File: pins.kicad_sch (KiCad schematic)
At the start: 10 parts, among them J2 AXK640347YG, J3 Conn_01x09, J6 Conn_01x40_Pin

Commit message: initial commit, not complete.
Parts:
- added C36, C37: 100n, Capacitor_SMD:C_0603_1608Metric_Pad1.08x0.95mm_HandSolder, symbol Device:C_Small
- added H1, H2, H3, H4: MountingHole_Pad, MountingHole:MountingHole_2.7mm_M2.5_DIN965_Pad_TopBottom, symbol Mechanical:MountingHole_Pad
- added JP1: Jumper_3_Open, Jumper:SolderJumper-3_P1.3mm_Open_RoundedPad1.0x1.5mm_NumberLabels, symbol Jumper:Jumper_3_Open
- added R30: 22k, Resistor_SMD:R_0603_1608Metric_Pad0.98x0.95mm_HandSolder, symbol Device:R_Small
- added R31: 12k, Resistor_SMD:R_0603_1608Metric_Pad0.98x0.95mm_HandSolder, symbol Device:R_Small
- added TP13: GP, TestPoint:TestPoint_Pad_D1.0mm, symbol Connector:TestPoint
- added U11: TXS0108EPW, Package_SO:TSSOP-20_4.4x6.5mm_P0.65mm, symbol Logic_LevelTranslator:TXS0108EPW
- added U8: TXS0102DCU, Package_SO:VSSOP-8_2.3x2mm_P0.5mm, symbol Logic_LevelTranslator:TXS0102DCU
- FB1: footprint Inductor_SMD:L_0603_1608Metric_Pad1.05x0.95mm_HandSolder -> Inductor_SMD:L_0805_2012Metric_Pad1.15x1.40mm_HandSolder
- J2: now not fitted; now left out of the parts list
- J3: footprint Connector_PinSocket_2.00mm:PinSocket_1x09_P2.00mm_Horizontal -> Connector_PinHeader_2.54mm:PinHeader_1x09_P2.54mm_Vertical; now fitted
- J6: now fitted; now in the parts list
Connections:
- net DISCAUDIO is gone; now on net BASEBAND_IN: J6.7 (Pin_7)
- net +5V: now also C37.1, U11.19 (VCCB), U8.7 (VCCB)
- net +5VD: now also J3.7 (Pin_7); no longer J3.2 (Pin_2)
- net 9V3: now also J6.38 (Pin_38)
- net AUDIO_IN: now also J3.4 (Pin_4), J6.33 (Pin_33); no longer J3.5 (Pin_5)
- net AUDIO_OUT_FILT: now also J3.3 (Pin_3), J6.34 (Pin_34); no longer J3.6 (Pin_6)
- net BASEBAND_IN: now also J3.2 (Pin_2); no longer J3.7 (Pin_7)
- net BASEBAND_OUT_FILT: now also J3.5 (Pin_5), JP1.2 (C); no longer J3.4 (Pin_4)
- net CH_Activity: now also U11.3 (A2); no longer J6.8 (Pin_8)
- net GND: now also J3.1 (Pin_1), C36.2, C37.2, H1.1, H2.1, H3.1, H4.1, R30.2, U11.11 (GND), U8.2 (GND); no longer J3.8 (Pin_8)
- net MCU_RX: now also TP13.1, U11.1 (A1), U8.5 (A1); no longer J3.1 (Pin_1)
- net OPT_CS: now also U11.9 (A8); no longer J6.30 (Pin_30)
- net PTT_IN: now also U11.7 (A6); no longer J3.9 (Pin_9)
- net PTT_OUT: now also U11.4 (A3), U8.4 (A2); no longer J3.3 (Pin_3)
- net RDY: now also U11.8 (A7); no longer J6.29 (Pin_29)
- net EXP_BD_REQ_5V: now reaches J6.10 (Pin_10)
- net EXP_BD_REQ_5V: now also U11.16 (B4)
- net EXP1_CS_5V: now reaches J6.11 (Pin_11)
- net EXP1_CS_5V: now also R31.2
- net GP4_IN_OUT_ACC8_5V: now reaches J6.12 (Pin_12)
- net GP4_IN_OUT_ACC8_5V: now also U11.15 (B5)
- net PTT_IN_5V: now reaches J6.23 (Pin_23)
- net PTT_IN_5V: now also U11.14 (B6)
- net Flat_Tx_Rtn: now reaches J6.31 (Pin_31)
- net Flat_Tx_Rtn: now also JP1.1 (A)
- net Tx_Aud_Rtn: now reaches J6.32 (Pin_32)
- net Tx_Aud_Rtn: now also JP1.3 (B)
- net GP1_IN_ACC3_5V: now reaches J6.9 (Pin_9)
- net GP1_IN_ACC3_5V: now also U11.17 (B3)
- net BUS+ renamed BUS+_5V
- net BUS+_5V: now also U11.20 (B1)
- new net: J3.6 (Pin_6), U8.1 (B2)
- new net: J3.8 (Pin_8), U8.8 (B1)
- new net +3V3: C36.1, U11.10 (OE), U11.2 (VCCA), U8.3 (VCCA), U8.6 (OE)
- new net CH_Activity_5V: J6.8 (Pin_8), U11.18 (B2)
- new net EXP1_CS: R30.1, R31.1
- new net EXP_BD_REQ: U11.5 (A4)
- new net GP4_IN_OUT_ACC8: U11.6 (A5)
- new net OPT_CS_5V: J6.30 (Pin_30), U11.12 (B8)
- new net RDY_5V: J6.29 (Pin_29), U11.13 (B7)
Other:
- note added: "All digital signals = 5V"
- note added: "VS_MIC VS_CS 9V3 VDD VS_AUDSEL Det_Aud_Snd Rx_Aud_Rtn Tx_Aud_Snd Tx_Aud_Rtn Flat_Tx_Rtn Opt_Bd_En Rdy/Req Rx_Aud_Snd ON INT_EXT_Vdd Key_Row Key_Col PTT Key_Intrp VS_INT RST* LED_EN OFF_BATT_DATA_OUT VS_GAINSEL SrD_Rtn SrD_Snd R/W* CS* DB0 DB1 DB2 DB3 EXT_BD_PTT DB4 DB5 145mV RMS @25kHz / 72mV RMS @12.5kHz DB6 DB7 A0 SCK_Snd VS_RAC Gnd, Pysically close pin to case"
- moved on the sheet: FB1, TP10, TP5, TP6, TP7, TP8, TP9

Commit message: .
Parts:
- removed TP10, TP13, TP6, TP8, TP9: GP, TestPoint:TestPoint_Pad_D1.0mm, symbol Connector:TestPoint
- added Q1: BC817, Package_TO_SOT_SMD:SOT-23, symbol Transistor_BJT:BC817
- added R32: 3k3, Resistor_SMD:R_0603_1608Metric_Pad0.98x0.95mm_HandSolder, symbol Device:R_Small
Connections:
- net +5VD: no longer TP5.1
- net GND: now also Q1.2 (E)
- net MCU_RX: now also TP5.1
- net at J3.9 (Pin_9): now also Q1.3 (C)
- new net: Q1.1 (B), R32.2
- new net BASEBAND_BYPASS: R32.1

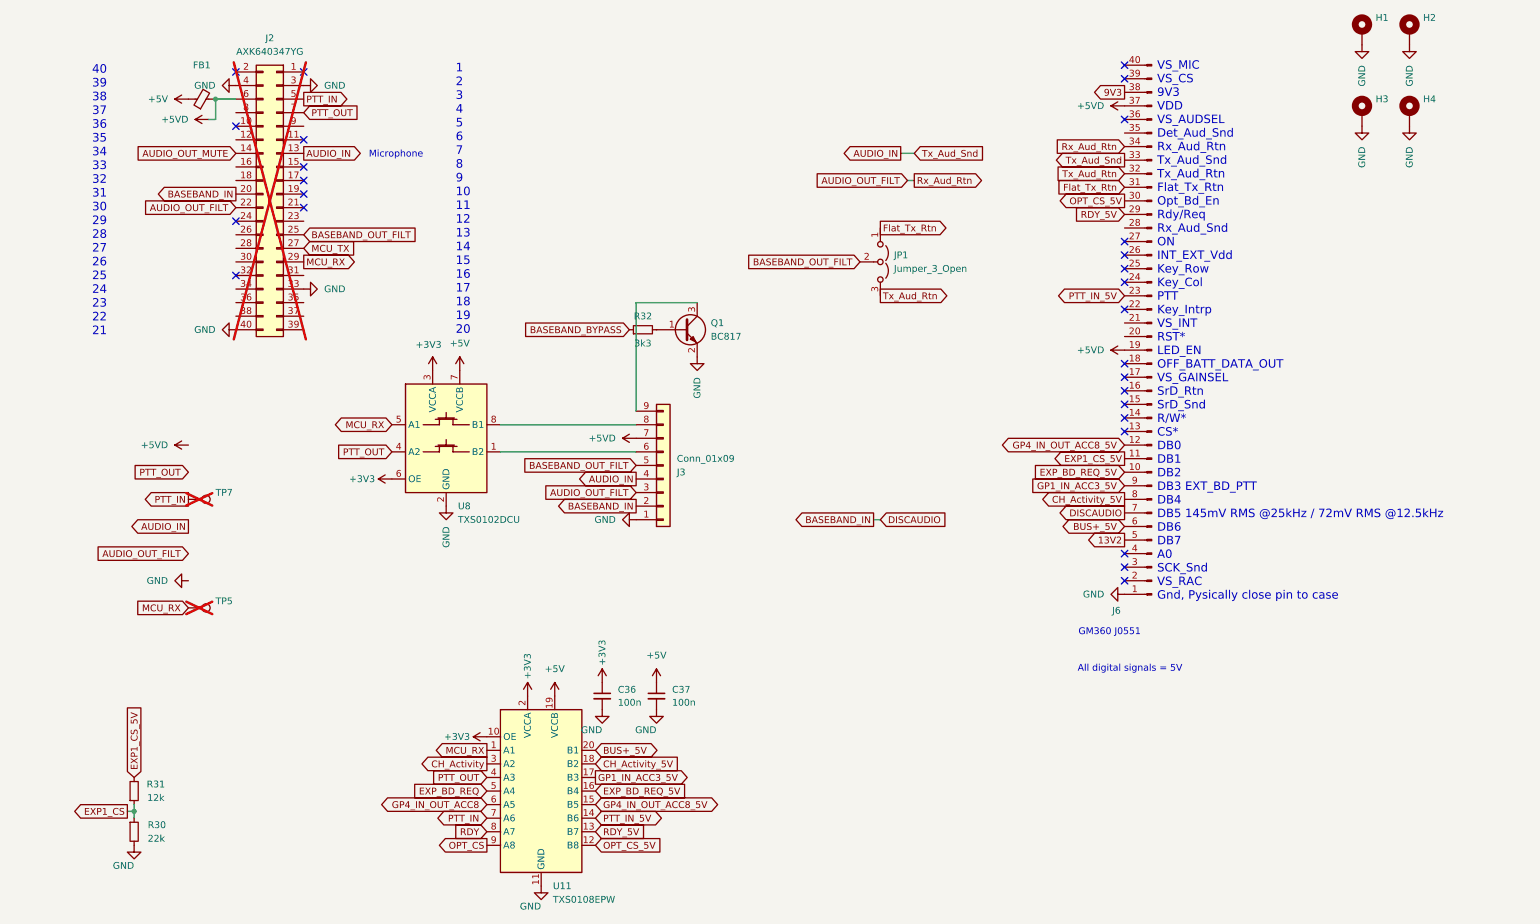
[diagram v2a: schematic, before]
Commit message: PCB shape is created. Most of routing done.
Todo: assign pins for radio control signals.
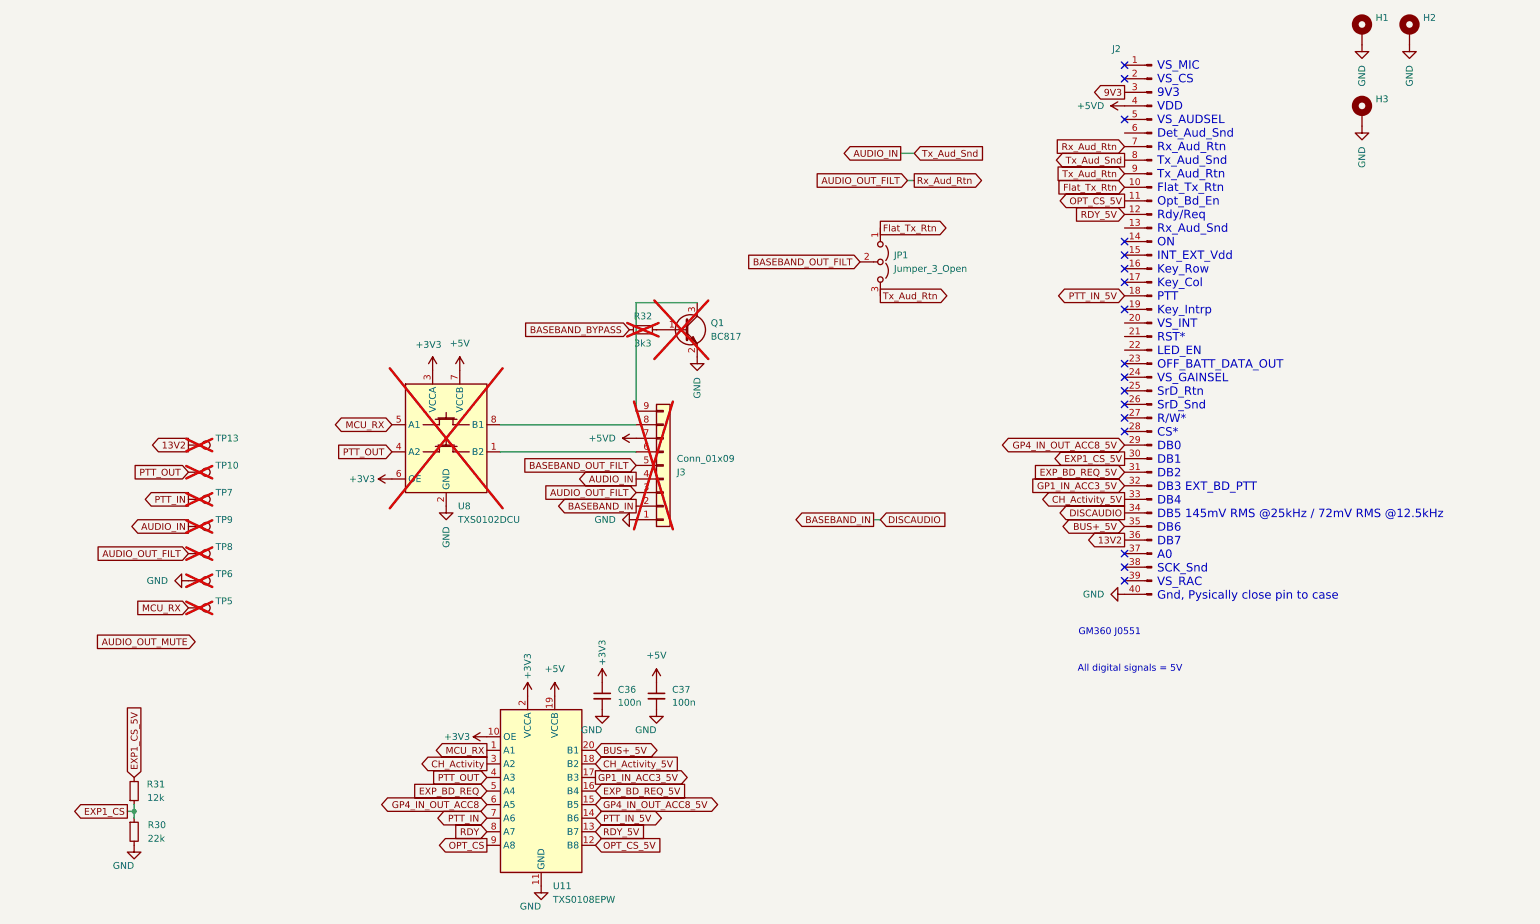
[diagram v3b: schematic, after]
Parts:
- removed FB1: FerriteBead_Small, Inductor_SMD:L_0805_2012Metric_Pad1.15x1.40mm_HandSolder, symbol Device:FerriteBead_Small
- removed H4: MountingHole_Pad, MountingHole:MountingHole_2.7mm_M2.5_DIN965_Pad_TopBottom, symbol Mechanical:MountingHole_Pad
- removed J2: AXK640347YG, micro17:AXK640347YG, symbol Connector_Generic:Conn_02x20_Odd_Even
- added TP10, TP13, TP6, TP8, TP9: GP, TestPoint:TestPoint_Pad_D1.0mm, symbol Connector:TestPoint
- J3: now not fitted
- Q1, R32, U8: now not fitted; now left out of the parts list
- renumbered J6 to J2
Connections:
- net +5VD: now also J2.4 (Pin_4); no longer J2.19 (Pin_19), J2.37 (Pin_37)
- net 13V2: now also J2.36 (Pin_36), TP13.1; no longer J2.5 (Pin_5)
- net 9V3: now also J2.3 (Pin_3); no longer J2.38 (Pin_38)
- net AUDIO_IN: now also J2.8 (Pin_8), TP9.1; no longer J2.33 (Pin_33)
- net AUDIO_OUT_FILT: now also J2.7 (Pin_7), TP8.1; no longer J2.34 (Pin_34)
- net BASEBAND_IN: now also J2.34 (Pin_34); no longer J2.7 (Pin_7)
- net BUS+_5V: now also J2.35 (Pin_35); no longer J2.6 (Pin_6)
- net CH_Activity_5V: now also J2.33 (Pin_33); no longer J2.8 (Pin_8)
- net EXP1_CS_5V: now also J2.30 (Pin_30); no longer J2.11 (Pin_11)
- net EXP_BD_REQ_5V: now also J2.31 (Pin_31); no longer J2.10 (Pin_10)
- net Flat_Tx_Rtn: now also J2.10 (Pin_10); no longer J2.31 (Pin_31)
- net GND: now also J2.40 (Pin_40), TP6.1; no longer J2.1 (Pin_1)
- net GP1_IN_ACC3_5V: now also J2.32 (Pin_32); no longer J2.9 (Pin_9)
- net GP4_IN_OUT_ACC8_5V: now also J2.29 (Pin_29); no longer J2.12 (Pin_12)
- net OPT_CS_5V: now also J2.11 (Pin_11); no longer J2.30 (Pin_30)
- net PTT_IN_5V: now also J2.18 (Pin_18); no longer J2.23 (Pin_23)
- net PTT_OUT: now also TP10.1
- net RDY_5V: now also J2.12 (Pin_12); no longer J2.29 (Pin_29)
- net Tx_Aud_Rtn: now also J2.9 (Pin_9); no longer J2.32 (Pin_32)
- no-connect marks 27 -> 17
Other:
- note removed: "1 2 3 4 5 6 7 8 9 10 11 12 13 14 15 16 17 18 19 20"
- note removed: "40 39 38 37 36 35 34 33 32 31 30 29 28 27 26 25 24 23 22 21"
- note removed: "Microphone"
- moved on the sheet: J2

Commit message: end of day commit
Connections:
- net RDY is gone; now on net AUDIO_OUT_MUTE: U11.8 (A7)
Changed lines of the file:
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@@
+		)
+	)
+	(global_label "AUDIO_OUT_MUTE"
+		(shape input)
+		(at 100.33 171.45 180)
+		(fields_autoplaced yes)
+		(effects
+			(font
+				(size 1.27 1.27)
+			)
+			(justify right)
+		)
+		(property "Intersheetrefs" "${INTERSHEET_REFS}"
+			(at 81.2581 171.45 0)
+			(effects
+				(font
+					(size 1.27 1.27)
+				)
+				(justify right)
+				(hide yes)
+			)
 		)
 	)
@@
 			(effects
 				(font
-					(size 1.27 1.27)
-				)
-				(justify right)
-				(hide yes)
-			)
-		)
-	)
-	(global_label "RDY"
-		(shape input)
-		(at 100.33 171.45 180)
-		(fields_autoplaced yes)
-		(effects
-			(font
-				(size 1.27 1.27)
-			)
-			(justify right)
-		)
-		(property "Intersheetrefs" "${INTERSHEET_REFS}"
-			(at 93.7162 171.45 0)
-			(effects
-				(font

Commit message: end of day commit
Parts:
- removed J3: Conn_01x09, Connector_PinHeader_2.54mm:PinHeader_1x09_P2.54mm_Vertical, symbol Connector_Generic:Conn_01x09
- removed U8: TXS0102DCU, Package_SO:VSSOP-8_2.3x2mm_P0.5mm, symbol Logic_LevelTranslator:TXS0102DCU
- added Q4, Q5: BC817, Package_TO_SOT_SMD:SOT-23, symbol Transistor_BJT:BC817
- added R45, R46, R47, R48, R49, R50, R51, R53: 3k3, Resistor_SMD:R_0603_1608Metric_Pad0.98x0.95mm_HandSolder, symbol Device:R_Small
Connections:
- net GP4_IN_OUT_ACC8 is gone; now on net AUDIO_OUT_MUTE: U11.6 (A5)
- net AUDIO_OUT_MUTE: now also R49.1; no longer U11.8 (A7)
- net BUS+_5V: now also R45.2
- net CH_Activity: now also R46.1
- net CH_Activity_5V: now also R46.2
- net EXP1_CS: now also R31.2; no longer R31.1
- net EXP1_CS_5V: now also R31.1; no longer R31.2
- net EXP_BD_REQ: now also R48.1
- net EXP_BD_REQ_5V: now also R48.2
- net GND: now also Q4.2 (E), Q5.2 (E), R53.1
- net GP1_IN_ACC3_5V: now also Q4.3 (C)
- net GP4_IN_OUT_ACC8_5V: now also Q5.3 (C)
- net MCU_RX: now also R45.1
- net OPT_CS: now also R50.1, R53.2
- net OPT_CS_5V: now also R50.2
- net PTT_OUT: now also R47.1
- net RDY_5V: now also R51.2
- new net: Q4.1 (B), R47.2
- new net: Q5.1 (B), R49.2
- new net RDY: R51.1, U11.8 (A7)
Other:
- note added: "40 VS_MIC 39 VS_CS 38 9V3 37 VDD 36 VS_AUDSEL 35 Det_Aud_Snd 34 Rx_Aud_Rtn 33 Tx_Aud_Snd 32 Tx_Aud_Rtn 31 Flat_Tx_Rtn 30 Opt_Bd_En 29 Rdy/Req 28 Rx_Aud_Snd 27 ON 26 INT_EXT_Vdd 25 Key_Row 24 Key_Col 23 PTT 22 Key_Intrp 21 VS_INT 20 RST* 19 LED_EN 18 OFF_BATT_DATA_OUT 17 VS_GAINSEL 16 SrD_Rtn 15 SrD_Snd 14 R/W* 13 CS* 12 DB0 11 DB1 10 DB2 9 DB3 EXT_BD_PTT 8 DB4 7 DB5 145mV RMS @25kHz / 72mV RMS @1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"
- note added: "5V Tolerant Pins"
- note added: "Normal Mic Audio"
- note removed: "VS_MIC VS_CS 9V3 VDD VS_AUDSEL Det_Aud_Snd Rx_Aud_Rtn Tx_Aud_Snd Tx_Aud_Rtn Flat_Tx_Rtn Opt_Bd_En Rdy/Req Rx_Aud_Snd ON INT_EXT_Vdd Key_Row Key_Col PTT Key_Intrp VS_INT RST* LED_EN OFF_BATT_DATA_OUT VS_GAINSEL SrD_Rtn SrD_Snd R/W* CS* DB0 DB1 DB2 DB3 EXT_BD_PTT DB4 DB5 145mV RMS @25kHz / 72mV RMS @12.5kHz DB6 DB7 A0 SCK_Snd VS_RAC Gnd, Pysically close pin to case"
- moved on the sheet: C36, C37, Q1, R30, R31, R32, TP10, TP13, TP5, TP6, TP7, TP8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
